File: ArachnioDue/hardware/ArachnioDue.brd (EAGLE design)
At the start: 21.6 x 52.1 mm, 52 parts, among them J6 HEAD17-NOSS, Q1 12MHz, U1 SAM3SB-AU, U2 AP2111HA-3.3

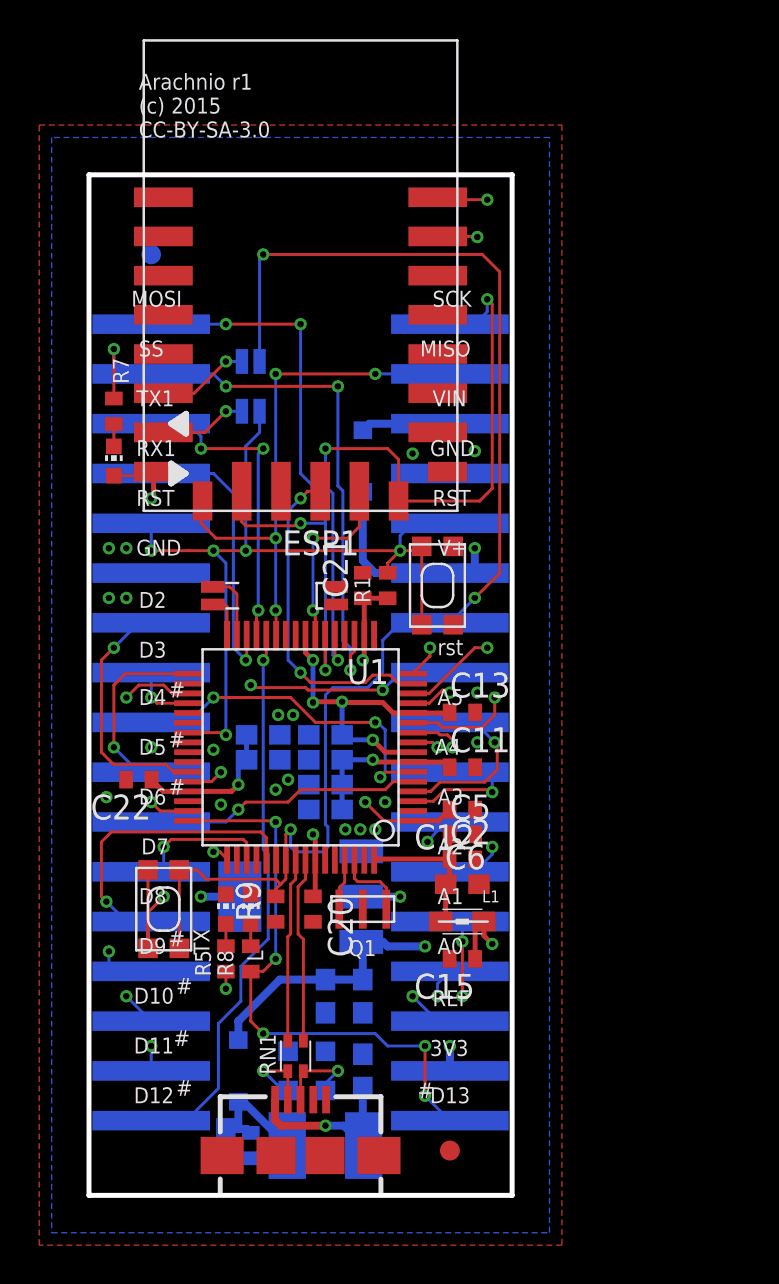
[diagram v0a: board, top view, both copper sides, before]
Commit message: Re-arranged features, added test points
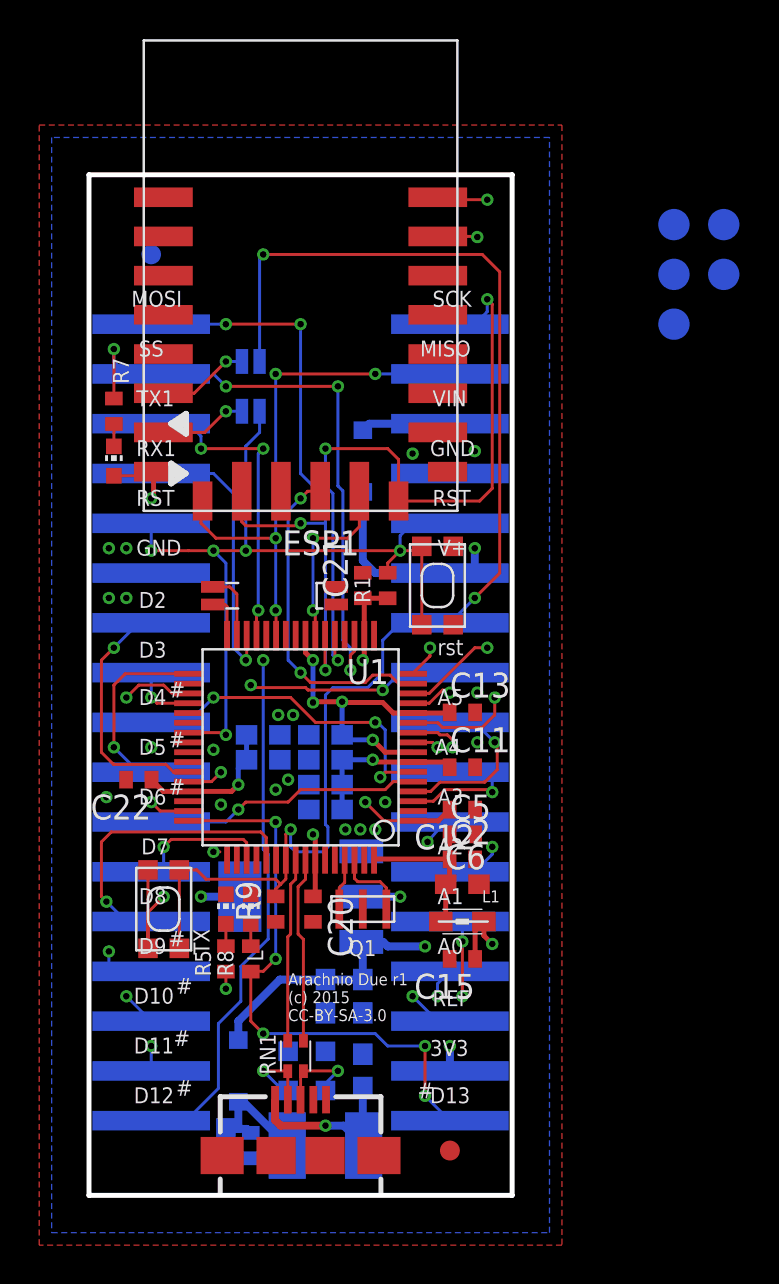
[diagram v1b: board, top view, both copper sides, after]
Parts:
- added TP1, TP2, TP3, TP4, TP5: PTR1TP16R, testpad:TP16R
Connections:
- net SWO renamed D14/SWO
- removed net RXTXLED/SS: J5.2, R7.1, U1.19
- new net RXTXLED: R7.1, U1.19
- new net SS: J5.2, U1.28
- net CHIP_EN: now also TP5.TP
- net D12: now also U1.37; no longer U1.28
- net D9: now also U1.26; no longer U1.35
- net ESP_CS: now also TP4.TP, U1.35; no longer U1.15
- net ESP_INT: now also TP3.TP
- net ESP_RESET: now also J6.5
- net ESP_RX: now also TP1.TP
- net ESP_TX: now also TP2.TP
- net RESET: no longer J6.5
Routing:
- net RXTXLED/SS: track 32.2 -> 0.00 mm, vias 4 -> 0
- net RXTXLED: track 0.00 -> 27.8 mm, vias 0 -> 4
- net RESET: track 43.3 -> 41.3 mm
- net D12: track 28.4 -> 27.3 mm
- net D9: track 20.0 -> 19.1 mm
- net ESP_CS: track 16.8 -> 16.1 mm
- net D14/SWO: track 20.8 -> 20.3 mm
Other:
- board text added: "Arachnio Due r1 (c) 2015 CC-BY-SA-3.0"
- board text removed: "Arachnio r1 (c) 2015 CC-BY-SA-3.0"
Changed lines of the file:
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@@
 <wire x1="57.15" y1="-39.37" x2="-39.37" y2="-39.37" width="0.254" layer="190"/>
 <wire x1="-39.37" y1="-39.37" x2="-39.37" y2="97.79" width="0.254" layer="190"/>
-<text x="0.635" y="53.975" size="0.8128" layer="25" ratio="17">Arachnio r1
+<text x="8.255" y="8.89" size="0.6096" layer="25" ratio="17">Arachnio Due r1
 (c) 2015
 CC-BY-SA-3.0</text>
@@
 <element name="RST_JMP" library="SparkFun-Passives" package="PAD-JUMPER-2-NO_YES_SILK" value="JUMPER-PAD-2-NOYES_SILK" x="6.35" y="40.005" rot="MR0"/>
 <element name="ERASE_JMP" library="SparkFun-Passives" package="PAD-JUMPER-2-NO_YES_SILK" value="JUMPER-PAD-2-NOYES_SILK" x="6.35" y="42.545" rot="MR180"/>
+<element name="TP1" library="testpad" package="TP16R" value="PTR1TP16R" x="27.94" y="49.53" rot="MR0">
+<attribute name="TP_SIGNAL_NAME" value="" x="27.94" y="49.53" size="1.778" layer="28" rot="MR0" display="off"/>
+</element>
+<element name="TP2" library="testpad" package="TP16R" value="PTR1TP16R" x="27.94" y="46.99" rot="MR0">
+<attribute name="TP_SIGNAL_NAME" value="" x="27.94" y="46.99" size="1.778" layer="28" rot="MR0" display="off"/>
+</element>
+<element name="TP3" library="testpad" package="TP16R" value="PTR1TP16R" x="27.94" y="44.45" rot="MR0">
+<attribute name="TP_SIGNAL_NAME" value="" x="27.94" y="44.45" size="1.778" layer="28" rot="MR0" display="off"/>
+</element>
+<element name="TP4" library="testpad" package="TP16R" value="PTR1TP16R" x="30.48" y="49.53" rot="MR0">
+<attribute name="TP_SIGNAL_NAME" value="" x="30.48" y="49.53" size="1.778" layer="28" rot="MR0" display="off"/>
+</element>
+<element name="TP5" library="testpad" package="TP16R" value="PTR1TP16R" x="30.48" y="46.99" rot="MR0">
+<attribute name="TP_SIGNAL_NAME" value="" x="30.48" y="46.99" size="1.778" layer="28" rot="MR0" display="off"/>
+</element>
 </elements>
 <signals>
@@
 <signal name="RESET">
 <contactref element="R1" pad="2"/>
-<contactref element="J6" pad="5"/>
 <contactref element="J5" pad="5"/>
 <contactref element="RESET" pad="4"/>
@@
 <wire x1="13.97" y1="32.893" x2="13.97" y2="33.655" width="0.1524" layer="16"/>
 <wire x1="13.97" y1="33.655" x2="14.605" y2="34.29" width="0.1524" layer="16"/>
-<wire x1="14.605" y1="34.29" x2="16.51" y2="34.29" width="0.1524" layer="16"/>
 <wire x1="13.97" y1="32.893" x2="14.732" y2="32.893" width="0.1524" layer="1"/>
 <wire x1="14.732" y1="32.893" x2="14.859" y2="33.02" width="0.1524" layer="1"/>
@@
 <signal name="D9">
 <contactref element="J5" pad="14"/>
-<contactref element="U1" pad="35"/>
-<wire x1="3.19" y1="25.61" x2="2.33" y2="25.61" width="0.1524" layer="1"/>
 <wire x1="2.33" y1="25.61" x2="1.905" y2="26.035" width="0.1524" layer="1"/>
 <wire x1="1.905" y1="26.035" x2="0.635" y2="26.035" width="0.1524" layer="1"/>
@@
 <wire x1="-0.889" y1="11.684" x2="-0.635" y2="11.43" width="0.1524" layer="16"/>
 <wire x1="-0.635" y1="11.43" x2="1.27" y2="11.43" width="0.1524" layer="16"/>
+<contactref element="U1" pad="26"/>
+<wire x1="2.33" y1="25.61" x2="8.14" y2="28.56" width="0" layer="19" extent="1-1"/>
 </signal>
 <signal name="D10">
@@
 <wire x1="8.89" y1="34.29" x2="10.16" y2="34.29" width="0.1524" layer="16"/>
 </signal>
-<signal name="RXTXLED/SS">
+<signal name="RXTXLED">
 <contactref element="R7" pad="1"/>
-<contactref element="J5" pad="2"/>
 <contactref element="U1" pad="19"/>
 <wire x1="-0.635" y1="40.655" x2="-0.635" y2="43.18" width="0.1524" layer="1"/>
@@
 <wire x1="-0.635" y1="43.18" x2="-0.635" y2="42.545" width="0.1524" layer="16"/>
 <wire x1="-0.635" y1="42.545" x2="0" y2="41.91" width="0.1524" layer="16"/>
-<wire x1="0" y1="41.91" x2="1.27" y2="41.91" width="0.1524" layer="16"/>
-<wire x1="1.27" y1="41.91" x2="4.445" y2="41.91" width="0.1524" layer="16"/>
 <wire x1="4.445" y1="41.91" x2="5.08" y2="41.275" width="0.1524" layer="16"/>
 <via x="5.08" y="41.275" extent="1-16" drill="0.3302"/>
@@
 <wire x1="11.64" y1="27.769" x2="11.43" y2="27.559" width="0.1524" layer="1"/>
 <wire x1="11.43" y1="27.559" x2="11.43" y2="26.797" width="0.1524" layer="1"/>
+<wire x1="4.445" y1="41.91" x2="0" y2="41.91" width="0" layer="19" extent="16-16"/>
 </signal>
 <signal name="N$3">
@@
 <signal name="D12">
 <contactref element="J5" pad="17"/>
-<contactref element="U1" pad="28"/>
-<wire x1="7.14" y1="28.56" x2="7.14" y2="27.46" width="0.1524" layer="1"/>
 <wire x1="7.14" y1="27.46" x2="6.985" y2="27.305" width="0.1524" layer="1"/>
 <via x="6.985" y="27.305" extent="1-16" drill="0.3302"/>
@@
 <wire x1="4.699" y1="5.461" x2="3.048" y2="3.81" width="0.1524" layer="16"/>
 <wire x1="1.27" y1="3.81" x2="3.048" y2="3.81" width="0.1524" layer="16"/>
+<contactref element="U1" pad="37"/>
+<wire x1="6.985" y1="27.305" x2="3.19" y2="24.61" width="0" layer="19" extent="1-1"/>
 </signal>
 <signal name="ERASE">
@@
 <wire x1="18.669" y1="12.827" x2="18.288" y2="12.827" width="0.254" layer="2"/>
 </signal>
-<signal name="SWO">
-<contactref element="U1" pad="49"/>
-<contactref element="J6" pad="8"/>
-<wire x1="16.51" y1="26.67" x2="13.97" y2="26.67" width="0.1524" layer="16"/>
-<wire x1="13.97" y1="26.67" x2="13.081" y2="25.781" width="0.1524" layer="16"/>
-<via x="13.081" y="25.781" extent="1-16" drill="0.3302"/>
-<wire x1="13.081" y1="25.781" x2="9.271" y2="25.781" width="0.1524" layer="1"/>
-<wire x1="9.271" y1="25.781" x2="9.144" y2="25.908" width="0.1524" layer="1"/>
-<wire x1="9.144" y1="25.908" x2="6.477" y2="25.908" width="0.1524" layer="1"/>
-<wire x1="6.477" y1="25.908" x2="6.35" y2="26.035" width="0.1524" layer="1"/>
-<via x="6.35" y="26.035" extent="1-16" drill="0.3302"/>
-<wire x1="6.35" y1="26.035" x2="6.35" y2="19.431" width="0.1524" layer="15"/>
-<wire x1="6.35" y1="19.431" x2="4.445" y2="17.526" width="0.1524" layer="15"/>
-<via x="4.445" y="17.526" extent="1-16" drill="0.3302"/>
-<wire x1="4.445" y1="17.526" x2="4.774" y2="17.526" width="0.1524" layer="1"/>
-<wire x1="4.774" y1="17.526" x2="5.14" y2="17.16" width="0.1524" layer="1"/>
-</signal>
 <signal name="SWCLK/D8">
 <contactref element="U1" pad="53"/>
@@
 <signal name="CHIP_EN">
 <contactref element="U1" pad="20"/>
+<contactref element="TP5" pad="TP"/>
+<wire x1="11.14" y1="28.56" x2="30.48" y2="46.99" width="0" layer="19" extent="1-16"/>
 </signal>
 <signal name="VCC">
@@
 <signal name="ESP_RESET">
 <contactref element="ESP1" pad="REST"/>
+<contactref element="J6" pad="5"/>
+<wire x1="16.51" y1="34.29" x2="1.89" y2="50.925" width="0" layer="19" extent="1-16"/>
 </signal>
 <signal name="ESP_LOAD">
@@
 <wire x1="18.796" y1="25.4" x2="18.796" y2="24.511" width="0.1524" layer="1"/>
 <wire x1="18.796" y1="24.511" x2="18.161" y2="23.876" width="0.1524" layer="1"/>
+<contactref element="TP1" pad="TP"/>
+<wire x1="18.542" y1="49.149" x2="27.94" y2="49.53" width="0" layer="19" extent="15-16"/>
 </signal>
 <signal name="ESP_TX">
@@
 <via x="18.415" y="27.94" extent="1-16" drill="0.3302"/>
 <wire x1="18.415" y1="27.94" x2="18.415" y2="43.942" width="0.1524" layer="15"/>
+<contactref element="TP2" pad="TP"/>
+<wire x1="18.415" y1="43.942" x2="27.94" y2="46.99" width="0" layer="19" extent="15-16"/>
 </signal>
 <signal name="ESP_CS">
 <contactref element="ESP1" pad="CS"/>
-<contactref element="U1" pad="15"/>
 <wire x1="9.89" y1="35.925" x2="9.255" y2="35.925" width="0.1524" layer="1"/>
 <wire x1="9.255" y1="35.925" x2="8.89" y2="35.56" width="0.1524" layer="1"/>
@@
 <wire x1="12.573" y1="26.543" x2="13.462" y2="26.543" width="0.1524" layer="1"/>
 <wire x1="13.462" y1="26.543" x2="13.895" y2="26.11" width="0.1524" layer="1"/>
-<wire x1="14.59" y1="26.11" x2="13.895" y2="26.11" width="0.1524" layer="1"/>
+<contactref element="U1" pad="35"/>
+<contactref element="TP4" pad="TP"/>
+<wire x1="9.89" y1="35.925" x2="30.48" y2="49.53" width="0" layer="19" extent="1-16"/>
+<wire x1="3.19" y1="25.61" x2="8.255" y2="27.305" width="0" layer="19" extent="1-16"/>
 </signal>
 <signal name="ESP_INT">
@@
 <wire x1="11.89" y1="35.925" x2="11.89" y2="34.115" width="0.1524" layer="1"/>
 <wire x1="11.89" y1="34.115" x2="11.303" y2="33.528" width="0.1524" layer="1"/>
+<contactref element="TP3" pad="TP"/>
+<wire x1="11.89" y1="35.925" x2="27.94" y2="44.45" width="0" layer="19" extent="1-16"/>
+</signal>
+<signal name="SS">
+<contactref element="U1" pad="28"/>
+<contactref element="J5" pad="2"/>
+<wire x1="7.14" y1="28.56" x2="1.27" y2="41.91" width="0" layer="19" extent="1-16"/>
+</signal>
+<signal name="D14/SWO">
+<contactref element="U1" pad="49"/>
+<contactref element="J6" pad="8"/>
+<wire x1="16.51" y1="26.67" x2="13.97" y2="26.67" width="0.1524" layer="16"/>
+<wire x1="13.97" y1="26.67" x2="13.081" y2="25.781" width="0.1524" layer="16"/>
+<via x="13.081" y="25.781" extent="1-16" drill="0.3302"/>
+<wire x1="13.081" y1="25.781" x2="9.271" y2="25.781" width="0.1524" layer="1"/>
+<wire x1="9.271" y1="25.781" x2="9.144" y2="25.908" width="0.1524" layer="1"/>
+<wire x1="9.144" y1="25.908" x2="6.477" y2="25.908" width="0.1524" layer="1"/>
+<wire x1="6.477" y1="25.908" x2="6.35" y2="26.035" width="0.1524" layer="1"/>
+<via x="6.35" y="26.035" extent="1-16" drill="0.3302"/>
+<wire x1="6.35" y1="26.035" x2="6.35" y2="19.431" width="0.1524" layer="15"/>
+<wire x1="6.35" y1="19.431" x2="4.445" y2="17.526" width="0.1524" layer="15"/>
+<via x="4.445" y="17.526" extent="1-16" drill="0.3302"/>
+<wire x1="4.445" y1="17.526" x2="4.774" y2="17.526" width="0.1524" layer="1"/>
+<wire x1="4.774" y1="17.526" x2="5.14" y2="17.16" width="0" layer="19" extent="1-1"/>
 </signal>
 </signals>

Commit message: Some last changes to the schematic and layout
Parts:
- moved TP4 22.9 mm to (8.89, 41.9), turned to 180 degrees
- moved TP1 22.2 mm to (6.35, 44.5), turned to 180 degrees
- moved TP5 19.7 mm to (11.4, 41.9), turned to 180 degrees
- moved TP3 19.1 mm to (8.89, 44.5), turned to 180 degrees
- moved TP2 16.7 mm to (11.4, 44.5), turned to 180 degrees
- moved R7 5.08 mm to (-0.64, 34.9), turned to 90 degrees
- moved Y2 0.90 mm to (3.17, 30.5)
- turned RX to 180 degrees
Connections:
- net RXTXLED: now also U1.34; no longer U1.19
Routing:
- net ESP_RESET: track 0.00 -> 31.3 mm, vias 0 -> 2
- net SS: track 0.00 -> 23.7 mm, vias 0 -> 2
- net ESP_RX: track 34.5 -> 50.5 mm, vias 2 -> 3
- net CHIP_EN: track 0.00 -> 13.8 mm, vias 0 -> 1
- net RXTXLED: track 27.8 -> 14.3 mm, vias 4 -> 2
- net ESP_INT: track 9.43 -> 19.8 mm, vias 2 -> 3
- net ESP_TX: track 28.6 -> 37.5 mm, vias 2 -> 3
- net D9: track 19.1 -> 27.9 mm
- net ESP_CS: track 16.1 -> 23.1 mm, vias 2 -> 3
- net MOSI: track 33.5 -> 28.2 mm
- net D0/RX: track 14.7 -> 12.3 mm
- net RESET: track 41.3 -> 39.7 mm
- net D12: track 27.3 -> 28.4 mm
- net ERASE: track 69.8 -> 68.8 mm, vias 3 -> 4
- net N$5: track 2.25 -> 3.15 mm
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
